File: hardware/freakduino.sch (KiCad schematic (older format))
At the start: 10 parts, among them U6 ATMEGA328-QFP32

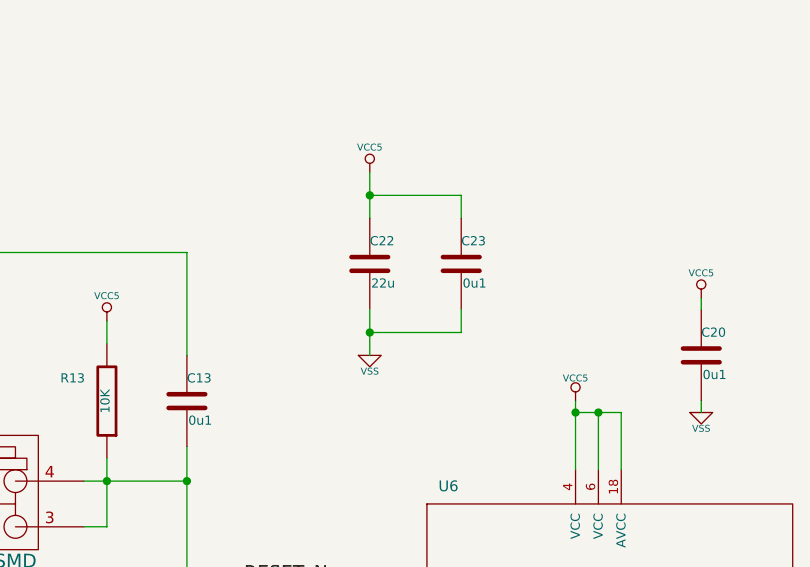
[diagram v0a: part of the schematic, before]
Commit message: Started PCB layout.
Board edges are done and most of the component modules are pre-placed.
There's a few decisions to make about substitute parts and custom
module drawing to be done accordingly.

Minor change to BOM files.
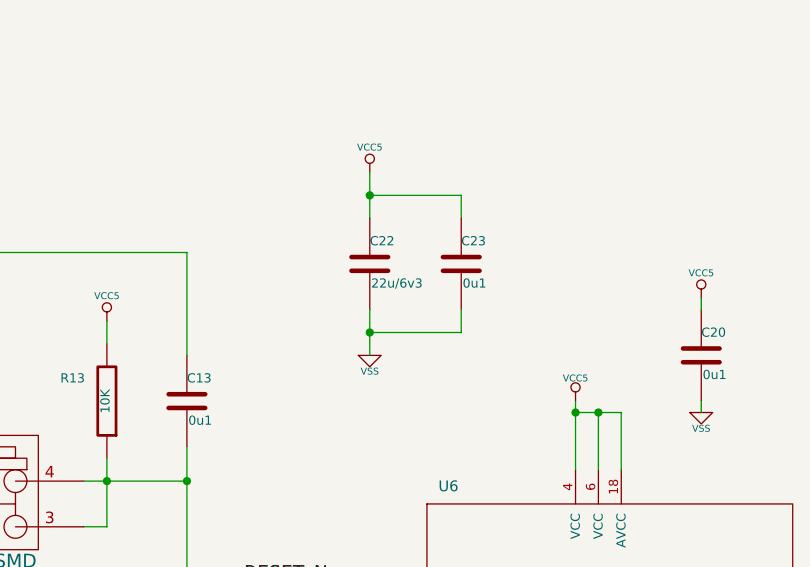
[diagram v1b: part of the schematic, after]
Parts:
- C22: value 22u -> 22u/6v3
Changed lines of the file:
@@
 P 6800 1750
 F 0 "C22" H 6800 1850 40  0000 L CNN
-F 1 "22u" H 6806 1665 40  0000 L CNN
+F 1 "22u/6v3" H 6806 1665 40  0000 L CNN
 F 2 "" H 6838 1600 30  0000 C CNN
 F 3 "" H 6800 1750 60  0000 C CNN
